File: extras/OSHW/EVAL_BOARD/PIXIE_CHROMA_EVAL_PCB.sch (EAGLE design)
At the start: 8 parts

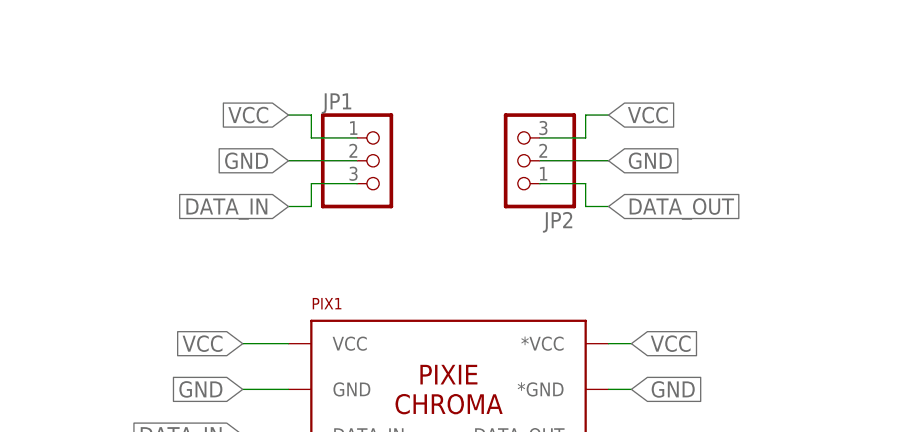
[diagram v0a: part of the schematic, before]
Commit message: Labeled schematic with license info
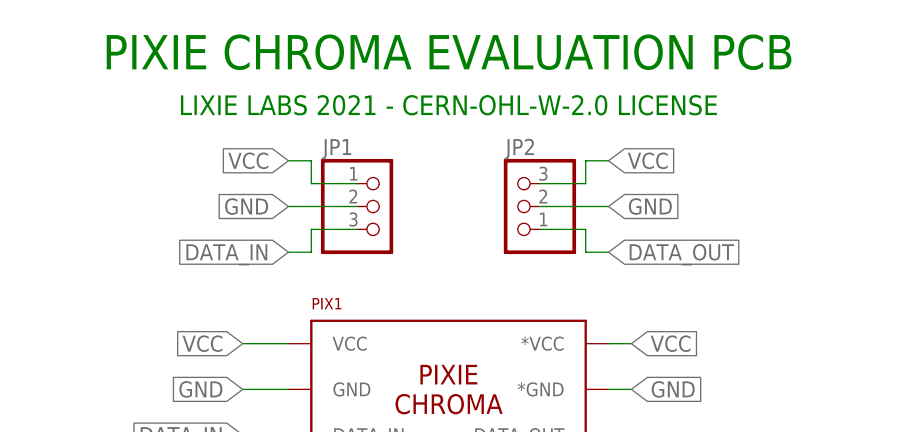
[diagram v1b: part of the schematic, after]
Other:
- note added: "LIXIE LABS 2021 - CERN-OHL-W-2.0 LICENSE"
- note added: "PIXIE CHROMA EVALUATION PCB"
- moved on the sheet: JP1, JP2
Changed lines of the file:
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@@
 <sheet>
 <plain>
+<text x="15.24" y="43.18" size="3.81" layer="91" align="bottom-center">PIXIE CHROMA EVALUATION PCB</text>
+<text x="15.24" y="38.1" size="2.1844" layer="91" align="bottom-center">LIXIE LABS 2021 - CERN-OHL-W-2.0 LICENSE</text>
 </plain>
 <instances>
@@
 <attribute name="NAME" x="0" y="-97.79" size="1.27" layer="94"/>
 </instance>
-<instance part="JP1" gate="A" x="7.62" y="33.02" smashed="yes">
-<attribute name="NAME" x="1.27" y="38.735" size="1.778" layer="95"/>
-<attribute name="VALUE" x="1.27" y="25.4" size="1.778" layer="96"/>
-</instance>
-<instance part="JP2" gate="A" x="22.86" y="33.02" smashed="yes" rot="R180">
-<attribute name="NAME" x="29.21" y="27.305" size="1.778" layer="95" rot="R180"/>
-<attribute name="VALUE" x="29.21" y="40.64" size="1.778" layer="96" rot="R180"/>
+<instance part="JP1" gate="A" x="7.62" y="27.94" smashed="yes">
+<attribute name="NAME" x="1.27" y="33.655" size="1.778" layer="95"/>
+<attribute name="VALUE" x="1.27" y="20.32" size="1.778" layer="96"/>
+</instance>
+<instance part="JP2" gate="A" x="22.86" y="27.94" smashed="yes" rot="R180">
+<attribute name="NAME" x="21.59" y="33.655" size="1.778" layer="95"/>
+<attribute name="VALUE" x="29.21" y="35.56" size="1.778" layer="96" rot="R180"/>
 </instance>
 </instances>
@@
 <segment>
 <pinref part="JP1" gate="A" pin="1"/>
-<wire x1="5.08" y1="35.56" x2="0" y2="35.56" width="0.1524" layer="91"/>
-<wire x1="0" y1="35.56" x2="0" y2="38.1" width="0.1524" layer="91"/>
-<wire x1="0" y1="38.1" x2="-2.54" y2="38.1" width="0.1524" layer="91"/>
-<label x="-2.54" y="38.1" size="1.778" layer="95" rot="R180" xref="yes"/>
+<wire x1="5.08" y1="30.48" x2="0" y2="30.48" width="0.1524" layer="91"/>
+<wire x1="0" y1="30.48" x2="0" y2="33.02" width="0.1524" layer="91"/>
+<wire x1="0" y1="33.02" x2="-2.54" y2="33.02" width="0.1524" layer="91"/>
+<label x="-2.54" y="33.02" size="1.778" layer="95" rot="R180" xref="yes"/>
 </segment>
 <segment>
 <pinref part="JP2" gate="A" pin="3"/>
-<wire x1="25.4" y1="35.56" x2="30.48" y2="35.56" width="0.1524" layer="91"/>
-<wire x1="30.48" y1="35.56" x2="30.48" y2="38.1" width="0.1524" layer="91"/>
-<wire x1="30.48" y1="38.1" x2="33.02" y2="38.1" width="0.1524" layer="91"/>
-<label x="33.02" y="38.1" size="1.778" layer="95" xref="yes"/>
+<wire x1="25.4" y1="30.48" x2="30.48" y2="30.48" width="0.1524" layer="91"/>
+<wire x1="30.48" y1="30.48" x2="30.48" y2="33.02" width="0.1524" layer="91"/>
+<wire x1="30.48" y1="33.02" x2="33.02" y2="33.02" width="0.1524" layer="91"/>
+<label x="33.02" y="33.02" size="1.778" layer="95" xref="yes"/>
 </segment>
 </net>
@@
 <segment>
 <pinref part="JP1" gate="A" pin="2"/>
-<wire x1="5.08" y1="33.02" x2="-2.54" y2="33.02" width="0.1524" layer="91"/>
-<label x="-2.54" y="33.02" size="1.778" layer="95" rot="R180" xref="yes"/>
+<wire x1="5.08" y1="27.94" x2="-2.54" y2="27.94" width="0.1524" layer="91"/>
+<label x="-2.54" y="27.94" size="1.778" layer="95" rot="R180" xref="yes"/>
 </segment>
 <segment>
 <pinref part="JP2" gate="A" pin="2"/>
-<wire x1="25.4" y1="33.02" x2="33.02" y2="33.02" width="0.1524" layer="91"/>
-<label x="33.02" y="33.02" size="1.778" layer="95" xref="yes"/>
+<wire x1="25.4" y1="27.94" x2="33.02" y2="27.94" width="0.1524" layer="91"/>
+<label x="33.02" y="27.94" size="1.778" layer="95" xref="yes"/>
 </segment>
 </net>
@@
 <segment>
 <pinref part="JP2" gate="A" pin="1"/>
-<wire x1="25.4" y1="30.48" x2="30.48" y2="30.48" width="0.1524" layer="91"/>
-<wire x1="30.48" y1="30.48" x2="30.48" y2="27.94" width="0.1524" layer="91"/>
-<wire x1="30.48" y1="27.94" x2="33.02" y2="27.94" width="0.1524" layer="91"/>
-<label x="33.02" y="27.94" size="1.778" layer="95" xref="yes"/>
+<wire x1="25.4" y1="25.4" x2="30.48" y2="25.4" width="0.1524" layer="91"/>
+<wire x1="30.48" y1="25.4" x2="30.48" y2="22.86" width="0.1524" layer="91"/>
+<wire x1="30.48" y1="22.86" x2="33.02" y2="22.86" width="0.1524" layer="91"/>
+<label x="33.02" y="22.86" size="1.778" layer="95" xref="yes"/>
 </segment>
 </net>
@@
 <segment>
 <pinref part="JP1" gate="A" pin="3"/>
-<wire x1="5.08" y1="30.48" x2="0" y2="30.48" width="0.1524" layer="91"/>
-<wire x1="0" y1="30.48" x2="0" y2="27.94" width="0.1524" layer="91"/>
-<wire x1="0" y1="27.94" x2="-2.54" y2="27.94" width="0.1524" layer="91"/>
-<label x="-2.54" y="27.94" size="1.778" layer="95" rot="R180" xref="yes"/>
-</segment>
-</net>
+<wire x1="5.08" y1="25.4" x2="0" y2="25.4" width="0.1524" layer="91"/>
+<wire x1="0" y1="25.4" x2="0" y2="22.86" width="0.1524" layer="91"/>
+<wire x1="0" y1="22.86" x2="-2.54" y2="22.86" width="0.1524" layer="91"/>
+<label x="-2.54" y="22.86" size="1.778" layer="95" rot="R180" xref="yes"/>
+</segment>
+</net>
